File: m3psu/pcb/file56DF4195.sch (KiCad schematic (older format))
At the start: 5 parts

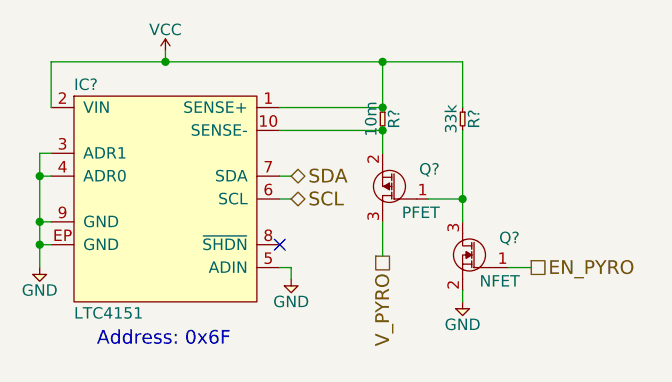
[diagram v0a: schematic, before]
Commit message: Changes in arrangement of schematic. Started wiring interconnects. WIP.
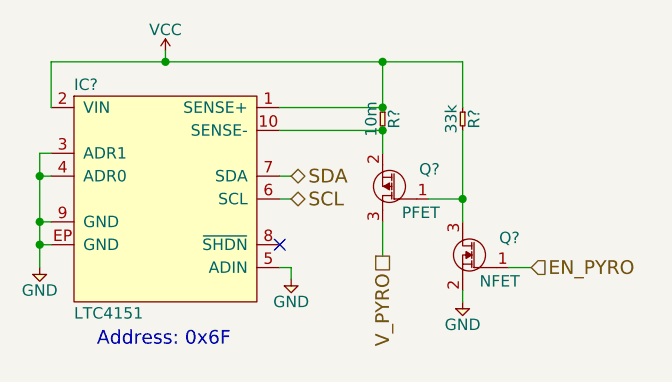
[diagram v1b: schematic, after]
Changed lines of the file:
@@
 $Descr A4 11693 8268
 encoding utf-8
-Sheet 12 12
+Sheet 12 13
 Title ""
 Date ""
@@
 	1    0    0    -1
 $EndComp
-Text HLabel 6050 3500 3    60   UnSpc ~ 0
-V_PYRO
 $Comp
 L R R?
@@
 	0    1    1    0
 $EndComp
-Text HLabel 6700 3550 2    60   UnSpc ~ 0
+Text HLabel 6700 3550 2    60   Input ~ 0
 EN_PYRO
 $Comp
@@
 	4600 3150 4550 3150
 Connection ~ 4550 3150
+Text HLabel 6050 3500 3    60   UnSpc ~ 0
+V_PYRO
 $EndSCHEMATC

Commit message: Grouped components, sorted internal interconnects. Sheets size now roughly proportional to number of components inside.
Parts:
- Q?: Farnell 2364070 -> 2490619
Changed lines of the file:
@@
 $Descr A4 11693 8268
 encoding utf-8
-Sheet 12 13
+Sheet 12 14
 Title ""
 Date ""
@@
 F 2 "" H 6400 3450 50  0001 C CNN
 F 3 "" H 6400 3450 50  0001 C CNN
-F 4 "2364070" H 6400 3450 60  0001 C CNN "Farnell"
+F 4 "2490619" H 6400 3450 60  0001 C CNN "Farnell"
 	1    6400 3450
 	-1   0    0    -1
